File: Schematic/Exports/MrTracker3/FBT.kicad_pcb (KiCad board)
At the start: 2 copper layers, 83.3 x 52 mm, 23 parts, among them J1 TRRS Connector 3.5, J2 TRRS Connector 3.5, SW1 SW_SPDT, U1 HT7333-1-TO92

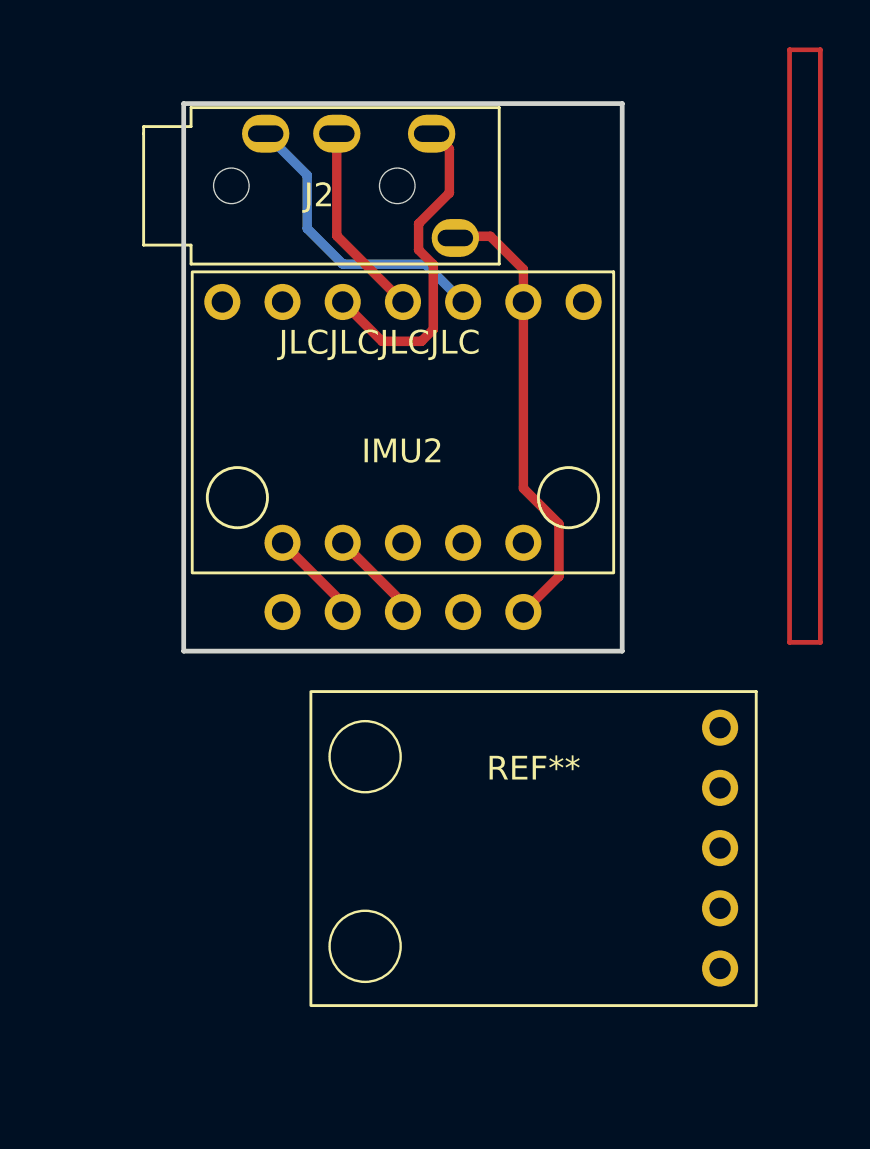
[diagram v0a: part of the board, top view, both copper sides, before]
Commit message: Export the next revision of PCBs for fabrication
Made at JLCPCB
Also picked apart the LSM6DS3 datasheet some more. Apparently, the auto hard/soft iron compensation isn't dynamic. It depends on pre-calculated matrices fed into the IMU's registers.
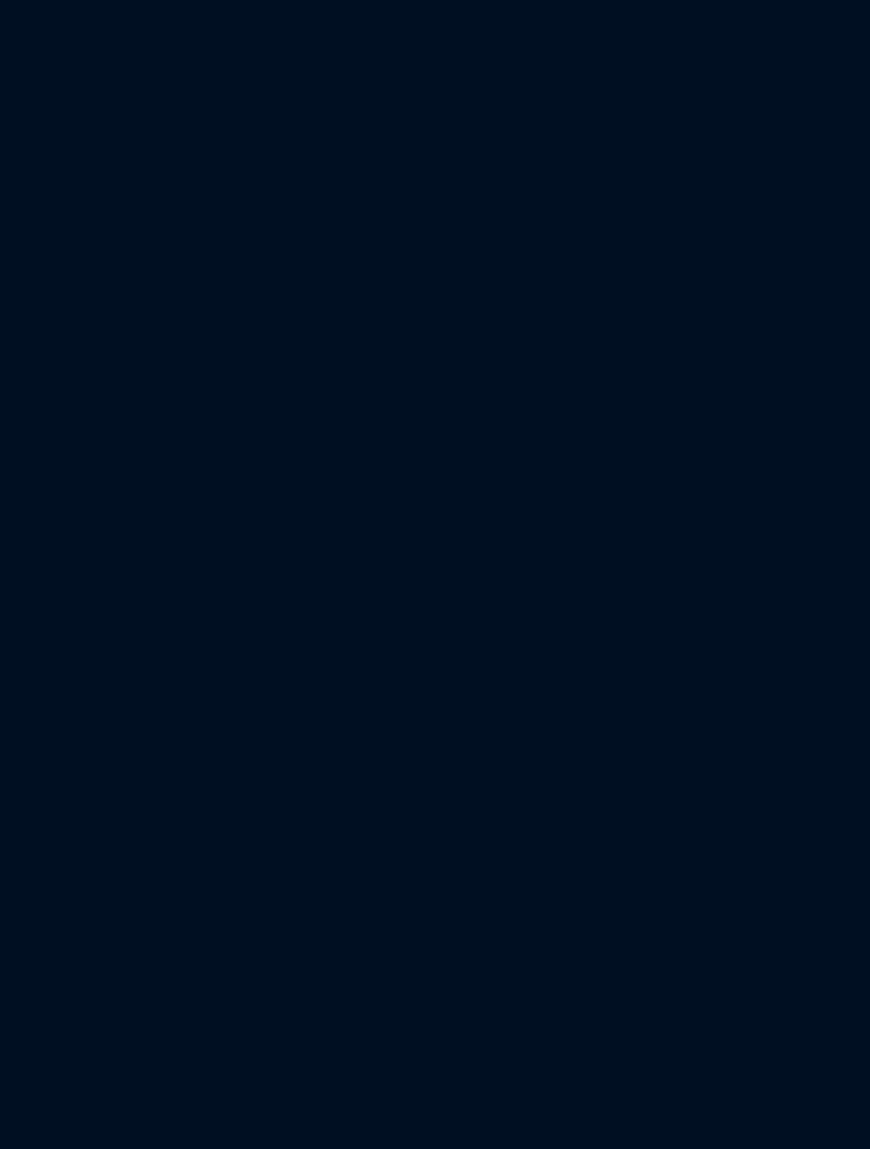
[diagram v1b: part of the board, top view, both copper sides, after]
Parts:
- removed GY2: ~, My_Library:GY-271
- removed IMU2: ~, My_Library:GY-BMI160
- removed J2: TRRS Connector 3.5, My_Library:PJ-320A
- removed the REF** at (176.5, 115.2)
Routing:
- net ESP32_3V3: track 122.6 -> 103.5 mm
- net SDA_1: track 64.0 -> 49.9 mm
- net GND: track 132.7 -> 120.1 mm
- net SCL_1: track 54.2 -> 45.9 mm
- net Net-(GY2-SDA): track 3.97 -> 0.00 mm
- net Net-(GY2-SCL): track 3.97 -> 0.00 mm
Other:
- board size 83.3 x 52 mm -> 40 x 40 mm
- board text removed: "UFBTM Type B Rev. 1.0"
